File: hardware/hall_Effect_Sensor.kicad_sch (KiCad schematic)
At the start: 3 parts

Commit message: Please Final Review
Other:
- note added: "HALL SIGNAL CLEANING"
- moved on the sheet: C24, R13, R14
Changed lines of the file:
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@@
 	(generator_version "10.0")
 	(paper "A4")
+	(rectangle
+		(start 121.92 80.01)
+		(end 186.69 101.6)
+		(stroke
+			(width 0)
+			(type default)
+		)
+		(fill
+			(type none)
+		)
+	)
+	(text "HALL SIGNAL CLEANING"
+		(exclude_from_sim no)
+		(at 138.176 77.47 0)
+		(effects
+			(font
+				(size 1.905 1.905)
+				(thickness 0.381)
+				(bold yes)
+			)
+		)
+	)
 	(junction
-		(at 115.57 80.01)
+		(at 158.75 83.82)
 		(diameter 0)
 		(color 0 0 0 0)
 	)
 	(junction
-		(at 111.76 90.17)
+		(at 154.94 93.98)
 		(diameter 0)
 		(color 0 0 0 0)
 	)
 	(junction
-		(at 106.68 80.01)
+		(at 149.86 83.82)
 		(diameter 0)
 		(color 0 0 0 0)
@@
 	(wire
 		(pts
-			(xy 105.41 80.01) (xy 106.68 80.01)
-		)
-		(stroke
-			(width 0)
-			(type default)
-		)
-	)
-	(wire
-		(pts
-			(xy 106.68 80.01) (xy 125.73 80.01)
-		)
-		(stroke
-			(width 0)
-			(type default)
-		)
-	)
-	(wire
-		(pts
-			(xy 106.68 90.17) (xy 115.57 90.17)
-		)
-		(stroke
-			(width 0)
-			(type default)
-		)
-	)
-	(wire
-		(pts
-			(xy 115.57 87.63) (xy 115.57 90.17)
-		)
-		(stroke
-			(width 0)
-			(type default)
-		)
-	)
-	(wire
-		(pts
-			(xy 111.76 90.17) (xy 111.76 93.98)
-		)
-		(stroke
-			(width 0)
-			(type default)
-		)
-	)
-	(wire
-		(pts
-			(xy 92.71 80.01) (xy 97.79 80.01)
-		)
-		(stroke
-			(width 0)
-			(type default)
-		)
-	)
-	(wire
-		(pts
-			(xy 106.68 90.17) (xy 106.68 87.63)
+			(xy 148.59 83.82) (xy 149.86 83.82)
+		)
+		(stroke
+			(width 0)
+			(type default)
+		)
+	)
+	(wire
+		(pts
+			(xy 149.86 83.82) (xy 168.91 83.82)
+		)
+		(stroke
+			(width 0)
+			(type default)
+		)
+	)
+	(wire
+		(pts
+			(xy 149.86 93.98) (xy 158.75 93.98)
+		)
+		(stroke
+			(width 0)
+			(type default)
+		)
+	)
+	(wire
+		(pts
+			(xy 158.75 91.44) (xy 158.75 93.98)
+		)
+		(stroke
+			(width 0)
+			(type default)
+		)
+	)
+	(wire
+		(pts
+			(xy 154.94 93.98) (xy 154.94 97.79)
+		)
+		(stroke
+			(width 0)
+			(type default)
+		)
+	)
+	(wire
+		(pts
+			(xy 135.89 83.82) (xy 140.97 83.82)
+		)
+		(stroke
+			(width 0)
+			(type default)
+		)
+	)
+	(wire
+		(pts
+			(xy 149.86 93.98) (xy 149.86 91.44)
 		)
 		(stroke
@@
 	(hierarchical_label "HALL_OUTPUT"
 		(shape output)
-		(at 125.73 80.01 0)
+		(at 168.91 83.82 0)
 		(effects
 			(font
@@
 	(hierarchical_label "GND"
 		(shape bidirectional)
-		(at 111.76 93.98 0)
+		(at 154.94 97.79 0)
 		(effects
 			(font
@@
 	(hierarchical_label "HALL_RAW"
 		(shape input)
-		(at 92.71 80.01 180)
+		(at 135.89 83.82 180)
 		(effects
 			(font
@@
 	(symbol
 		(lib_id "Device:R")
-		(at 101.6 80.01 90)
+		(at 144.78 83.82 90)
 		(unit 1)
 		(body_style 1)
@@
 		(dnp no)
 		(property "Reference" "R13"
-			(at 101.6 77.724 90)
+			(at 144.78 81.534 90)
 			(show_name no)
 			(do_not_autoplace no)
@@
 		)
 		(property "Value" "22k"
-			(at 101.854 80.01 90)
+			(at 145.034 83.82 90)
 			(show_name no)
 			(do_not_autoplace no)
@@
 		)
 		(property "Footprint" ""
-			(at 101.6 81.788 90)
+			(at 144.78 85.598 90)
 			(hide yes)
 			(show_name no)
@@
 		)
 		(property "Datasheet" ""
-			(at 101.6 80.01 0)
+			(at 144.78 83.82 0)
 			(hide yes)
 			(show_name no)
@@
 		)
 		(property "Description" "Resistor"
-			(at 101.6 80.01 0)
+			(at 144.78 83.82 0)
 			(hide yes)
 			(show_name no)
@@
 	(symbol
 		(lib_id "Device:C")
-		(at 115.57 83.82 0)
+		(at 158.75 87.63 0)
 		(unit 1)
 		(body_style 1)
@@
 		(fields_autoplaced yes)
 		(property "Reference" "C24"
-			(at 119.38 82.5499 0)
+			(at 162.56 86.3599 0)
 			(show_name no)
 			(do_not_autoplace no)
@@
 		)
 		(property "Value" "1nF"
-			(at 119.38 85.0899 0)
+			(at 162.56 88.8999 0)
 			(show_name no)
 			(do_not_autoplace no)
@@
 		)
 		(property "Footprint" ""
-			(at 116.5352 87.63 0)
+			(at 159.7152 91.44 0)
 			(hide yes)
 			(show_name no)
@@
 		)
 		(property "Datasheet" ""
-			(at 115.57 83.82 0)
+			(at 158.75 87.63 0)
 			(hide yes)
 			(show_name no)
@@
 		)
 		(property "Description" "Unpolarized capacitor"
-			(at 115.57 83.82 0)
+			(at 158.75 87.63 0)
 			(hide yes)
 			(show_name no)
@@
 	(symbol
 		(lib_id "Device:R")
-		(at 106.68 83.82 0)
+		(at 149.86 87.63 0)
 		(unit 1)
 		(body_style 1)
@@
 		(dnp no)
 		(property "Reference" "R14"
-			(at 108.458 83.82 0)
+			(at 151.638 87.63 0)
 			(show_name no)
 			(do_not_autoplace no)
@@
 		)
 		(property "Value" "10k"
-			(at 106.68 85.598 90)
+			(at 149.86 89.408 90)
 			(show_name no)
 			(do_not_autoplace no)
@@
 		)
 		(property "Footprint" ""
-			(at 104.902 83.82 90)
+			(at 148.082 87.63 90)
 			(hide yes)
 			(show_name no)
@@
 		)
 		(property "Datasheet" ""
-			(at 106.68 83.82 0)
+			(at 149.86 87.63 0)
 			(hide yes)
 			(show_name no)
@@
 		)
 		(property "Description" "Resistor"
-			(at 106.68 83.82 0)
-			(hide yes)
-			(show_name no)
+			(at 149.86 87.63 0)
+			(hide yes)
+			(show_name no)

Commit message: Ready for Final Schematic Review
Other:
- note added: "CUTOFF: 23MkHz"
- note added: "HALL SIGNAL CLEANING and VOLTAGE PULL DOWN"
- note removed: "HALL SIGNAL CLEANING"
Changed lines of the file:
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@@
 		)
 	)
-	(text "HALL SIGNAL CLEANING"
+	(text "CUTOFF: 23MkHz"
 		(exclude_from_sim no)
-		(at 138.176 77.47 0)
+		(at 177.038 99.822 0)
 		(effects
 			(font
+				(size 1.27 1.27)
+			)
+		)
+	)
+	(text "HALL SIGNAL CLEANING and VOLTAGE PULL DOWN"
+		(exclude_from_sim no)
+		(at 157.226 77.978 0)
+		(effects
+			(font

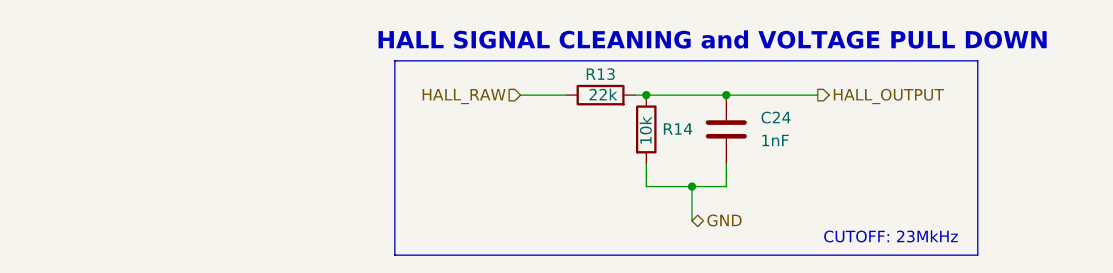
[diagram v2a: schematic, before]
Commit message: Changed MAG to SPI
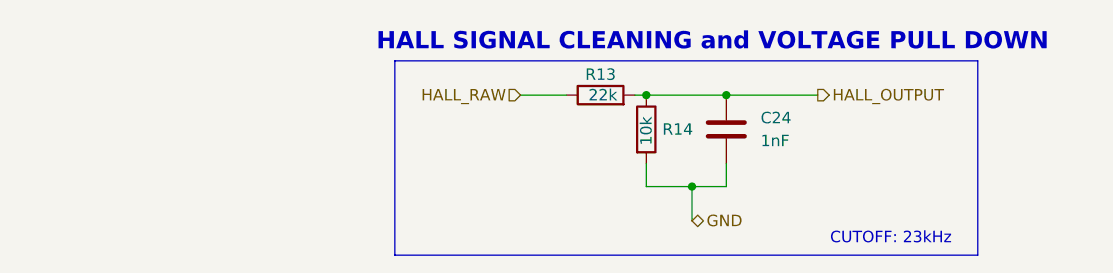
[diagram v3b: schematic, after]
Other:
- note added: "CUTOFF: 23kHz"
- note removed: "CUTOFF: 23MkHz"
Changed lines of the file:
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@@
 		)
 	)
-	(text "CUTOFF: 23MkHz"
+	(text "CUTOFF: 23kHz"
 		(exclude_from_sim no)
 		(at 177.038 99.822 0)
